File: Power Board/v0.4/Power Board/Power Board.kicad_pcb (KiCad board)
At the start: 4 copper layers, 70 x 80 mm, 84 parts, among them J1 Battery In, J2 JST B2PS-VH, J3 JST B2PS-VH, J4 JST B2PS-VH, J5 JST B2PS-VH, J6 JST B2PS-VH, J7 JST B2PS-VH, J9 Raspberry Pi, Q1 SI5504BDC, SW1 SW_Push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

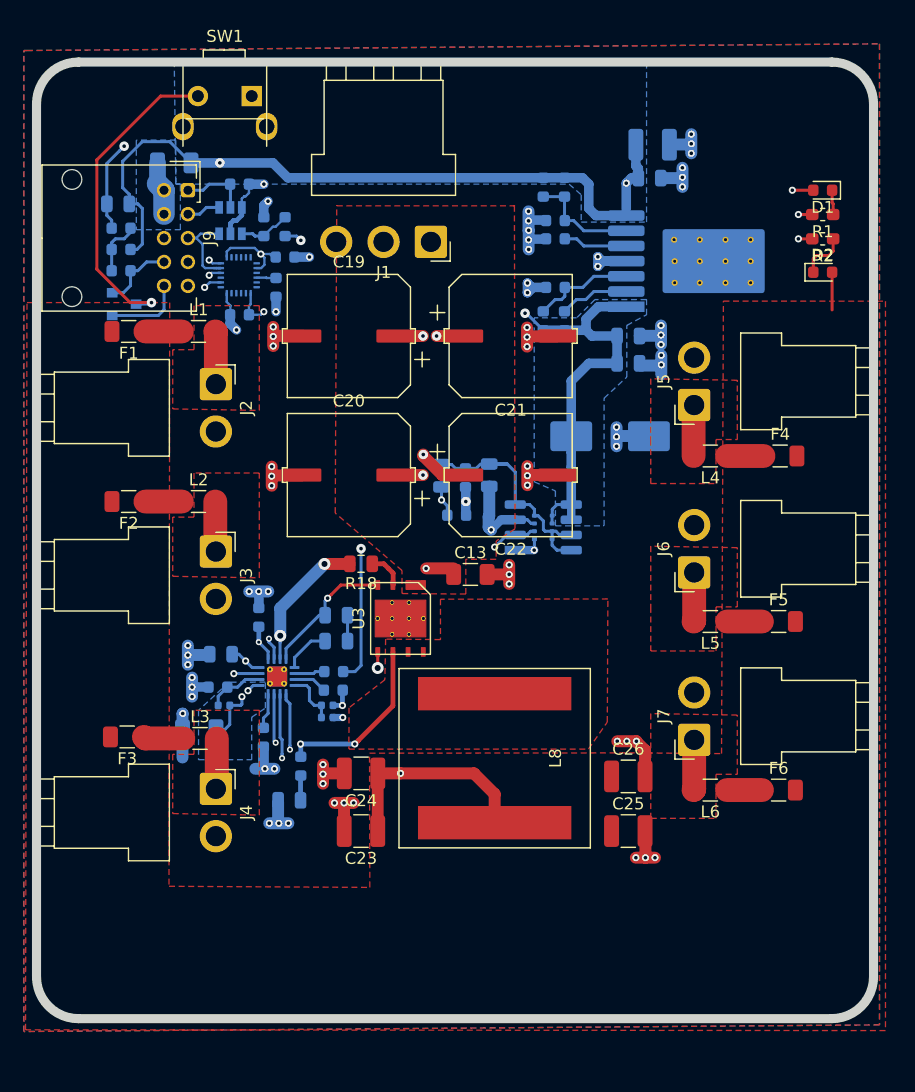
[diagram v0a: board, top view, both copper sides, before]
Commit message: Better ground flow through Q1 Need to add more copper for panel connector between fuse and ferrite
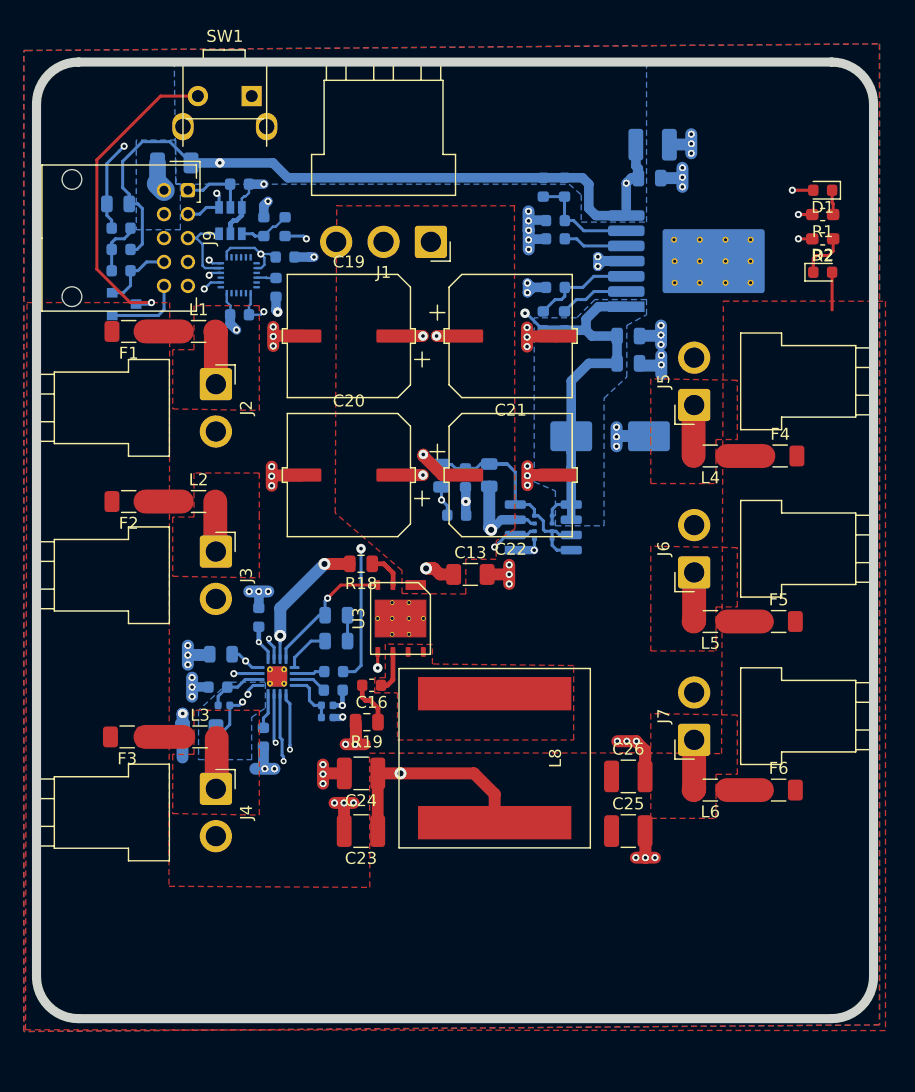
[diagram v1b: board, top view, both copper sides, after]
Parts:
- C16, R19: moved to F.Cu
- moved R19 9.20 mm to (104.6, 90.2)
- moved C16 8.99 mm to (105.0, 87.1), turned to 180 degrees
- moved L3 0.13 mm to (90.7, 91.4)
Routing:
- net SDA: track 78.1 -> 89.3 mm, vias 2 -> 3
- net /Panel Power/Switch_Node: track 14.7 -> 3.52 mm, vias 2 -> 0
- net Net-(C16-Pad2): track 2.60 -> 3.85 mm
- net /Panel_Power: track 43.3 -> 42.4 mm
- net /Battery_Power: track 45.9 -> 46.7 mm
- net Net-(C1-Pad1): track 21.5 -> 22.2 mm
- net GND: track 108.8 -> 109.4 mm, vias 76 -> 75

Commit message: Changed connections to panel connectors. Did some of the TLC work on the pours. Still need to fix DRC, mostly for U2 clearance issues that aren't really a DRC
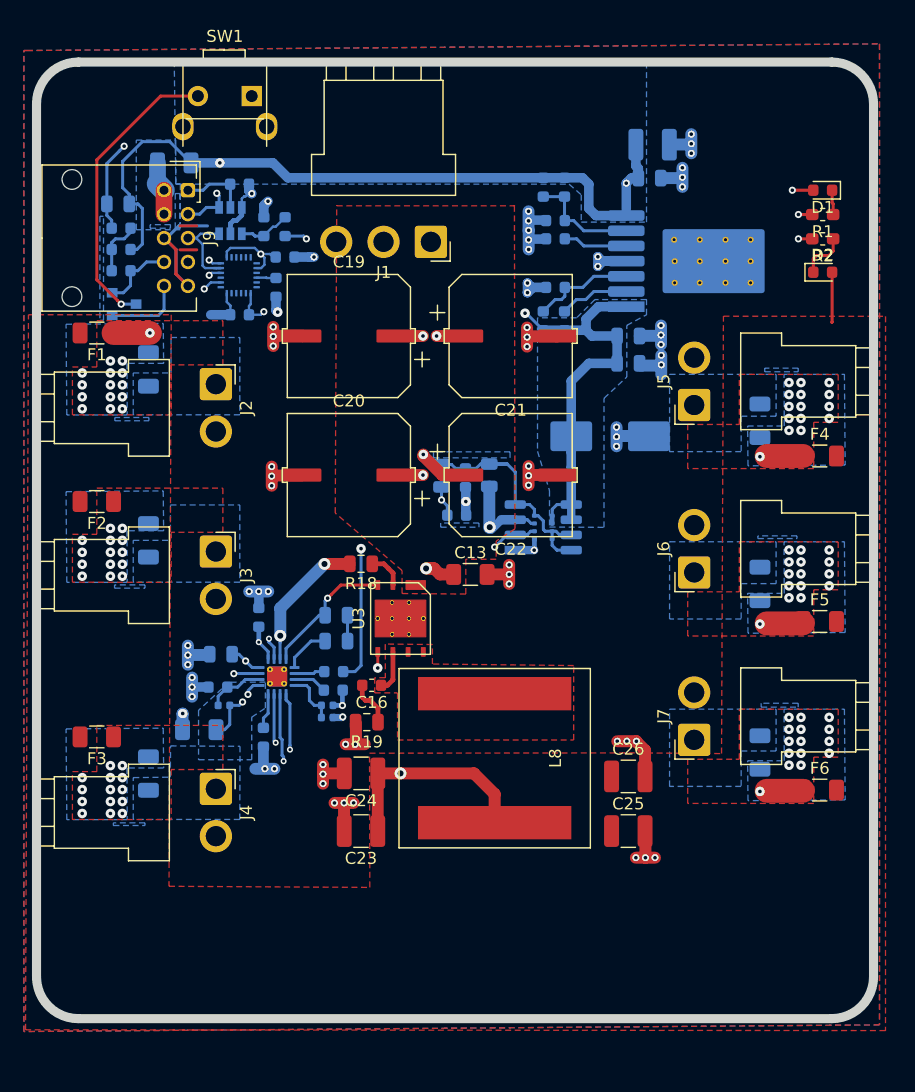
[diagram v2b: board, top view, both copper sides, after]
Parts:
- L1, L2, L3, L4, L5, L6: moved to B.Cu
- moved L2 5.30 mm to (86.4, 75.0), turned to 270 degrees
- moved L3 5.29 mm to (86.4, 94.5), turned to 270 degrees
- moved L1 5.26 mm to (86.4, 60.7), turned to 270 degrees
- moved L5 5.21 mm to (137.5, 78.6), turned to 90 degrees
- moved L6 5.21 mm to (137.5, 92.7), turned to 90 degrees
- moved L4 5.09 mm to (137.5, 65.0), turned to 90 degrees
- moved F5 3.44 mm to (142.5, 81.8)
- moved F6 3.44 mm to (142.5, 95.9)
- moved F4 3.31 mm to (142.5, 67.9)
- moved F1 2.67 mm to (82.0, 57.7)
- moved F2 2.67 mm to (82.0, 71.8)
- moved F3 2.54 mm to (82.0, 91.4)
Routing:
- net GND: track 109.4 -> 123.6 mm, vias 75 -> 74
- net Net-(J2-Pad1): track 4.43 -> 0.00 mm
- net Net-(J7-Pad1): track 4.22 -> 0.00 mm
- net Net-(J5-Pad1): track 4.28 -> 0.07 mm
- net Net-(J4-Pad1): track 4.24 -> 0.11 mm
- net Net-(J3-Pad1): track 4.20 -> 0.07 mm
- net Net-(J6-Pad1): track 4.12 -> 0.00 mm
- net Net-(F3-Pad1): track 3.17 -> 0.00 mm, vias 0 -> 14
- net Net-(F2-Pad1): track 3.04 -> 0.00 mm, vias 0 -> 14
- net /Pi Power/Power_Button: track 73.0 -> 70.9 mm
- net SCL: track 70.7 -> 68.9 mm
- net /Panel_Alert: track 57.6 -> 56.2 mm
- net /Panel_Power: track 42.4 -> 43.5 mm
- net SDA: track 89.3 -> 89.9 mm
- net Net-(F6-Pad1): track 2.91 -> 3.04 mm, vias 0 -> 15
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- added copper zone on B.Cu, net Net-(F1-Pad1)
- added copper zone on F.Cu, net Net-(F1-Pad1)
- added copper zone on B.Cu, net Net-(F2-Pad1)
- added copper zone on F.Cu, net Net-(F2-Pad1)
- added copper zone on B.Cu, net Net-(F3-Pad1)
- added copper zone on F.Cu, net Net-(F3-Pad1)
- added copper zone on B.Cu, net Net-(F4-Pad1)
- added copper zone on F.Cu, net Net-(F4-Pad1)
- added copper zone on B.Cu, net Net-(F5-Pad1)
- added copper zone on F.Cu, net Net-(F5-Pad1)
- added copper zone on B.Cu, net Net-(F6-Pad1)
- added copper zone on F.Cu, net Net-(F6-Pad1)
- added copper zone on B.Cu, net Net-(J2-Pad1)
- added copper zone on B.Cu, net Net-(J3-Pad1)
- added copper zone on B.Cu, net Net-(J4-Pad1)
- added copper zone on B.Cu, net Net-(J5-Pad1)
- added copper zone on B.Cu, net Net-(J6-Pad1)
- added copper zone on B.Cu, net Net-(J7-Pad1)
- removed copper zone on F.Cu, net Net-(J2-Pad1)
- removed copper zone on F.Cu, net Net-(J3-Pad1)
- removed copper zone on F.Cu, net Net-(J4-Pad1)
- removed copper zone on F.Cu, net Net-(J5-Pad1)
- removed copper zone on F.Cu, net Net-(J6-Pad1)
- removed copper zone on F.Cu, net Net-(J7-Pad1)
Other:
- net class U2 removed

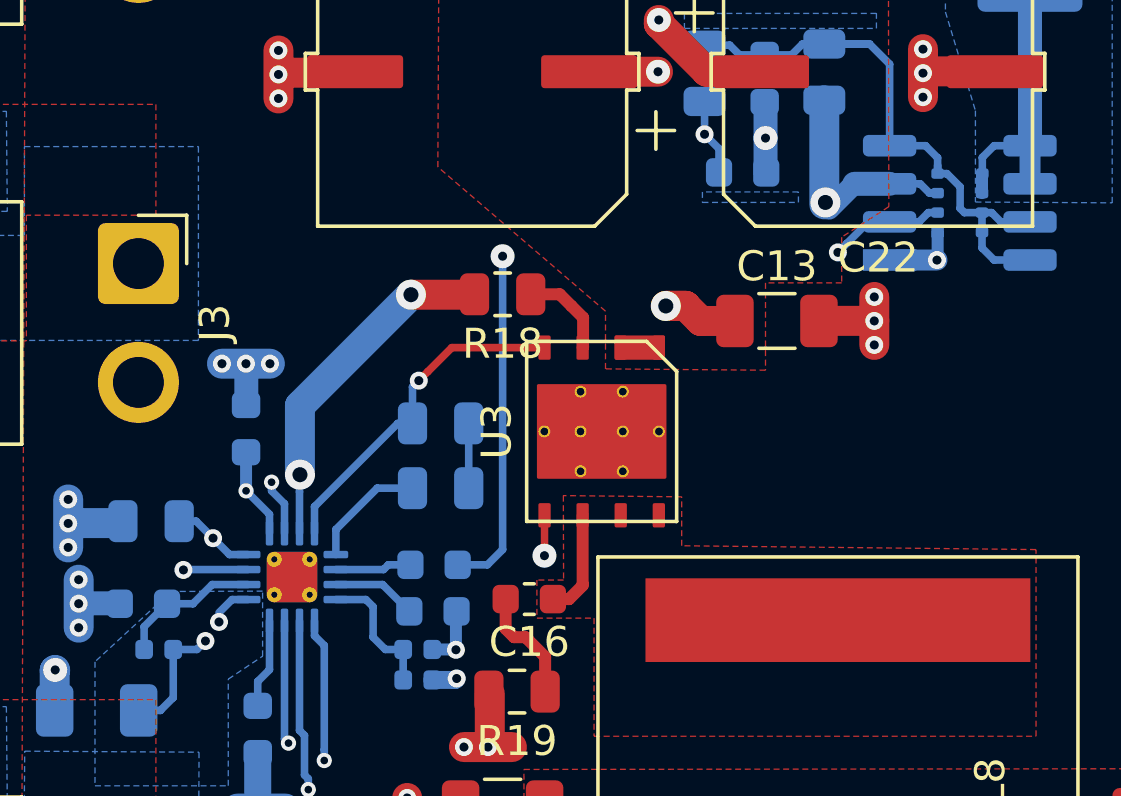
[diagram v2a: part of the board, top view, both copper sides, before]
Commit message: Tracks and rules tweaked to eliminate most DRC 2 DRC errors remain which don't seem valid
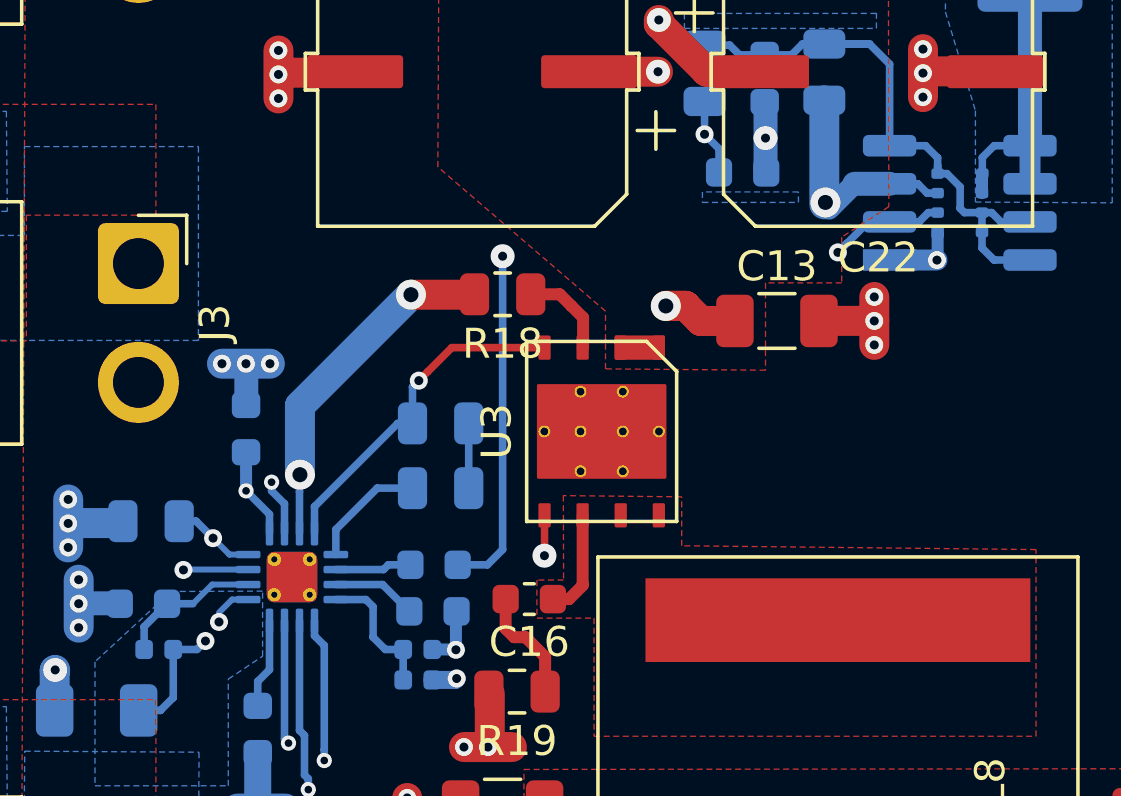
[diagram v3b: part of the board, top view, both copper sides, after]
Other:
- net class Pi_Battery: clearance 0.3 -> 0.25
- net class Pi_Power: clearance 0.3 -> 0.25
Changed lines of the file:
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@@
     (mod_text_size 1 1)
     (mod_text_width 0.15)
-    (pad_size 0.25 0.825)
-    (pad_drill 0)
+    (pad_size 0.45 0.45)
+    (pad_drill 0.2)
     (pad_to_mask_clearance 0.0508)
     (solder_mask_min_width 0.25)
@@
   )
   (net_class Pi_Battery ""
-    (clearance 0.3)
+    (clearance 0.25)
     (trace_width 0.3)
     (via_dia 1)
@@
   )
   (net_class Pi_Power ""
-    (clearance 0.3)
+    (clearance 0.25)
     (trace_width 1.4)
     (via_dia 1)
@@
     (pad 17 smd roundrect (at 0 0 90) (size 1.68 1.68) (layers F.Cu) (roundrect_rratio 0.14881)
       (net 4 GND) (zone_connect 2))
-    (pad 17 thru_hole circle (at 0.59 -0.59 90) (size 0.5 0.5) (drill 0.2) (layers *.Cu)
+    (pad 17 thru_hole circle (at 0.59 -0.59 90) (size 0.45 0.45) (drill 0.2) (layers *.Cu)
       (net 4 GND) (zone_connect 2))
-    (pad 17 thru_hole circle (at -0.59 -0.59 90) (size 0.5 0.5) (drill 0.2) (layers *.Cu)
+    (pad 17 thru_hole circle (at -0.59 -0.59 90) (size 0.45 0.45) (drill 0.2) (layers *.Cu)
       (net 4 GND) (zone_connect 2))
-    (pad 17 thru_hole circle (at 0.59 0.59 90) (size 0.5 0.5) (drill 0.2) (layers *.Cu)
+    (pad 17 thru_hole circle (at 0.59 0.59 90) (size 0.45 0.45) (drill 0.2) (layers *.Cu)
       (net 4 GND) (zone_connect 2))
-    (pad 17 thru_hole circle (at -0.59 0.59 90) (size 0.5 0.5) (drill 0.2) (layers *.Cu)
+    (pad 17 thru_hole circle (at -0.59 0.59 90) (size 0.45 0.45) (drill 0.2) (layers *.Cu)
       (net 4 GND) (zone_connect 2))
     (pad 17 smd roundrect (at 0 0 90) (size 1.68 1.68) (layers B.Cu B.Mask) (roundrect_rratio 0.14881)
@@
   (segment (start 107.024 57.912) (end 109.32 57.912) (width 1) (layer F.Cu) (net 3))
   (segment (start 107.024 69.542) (end 109.32 69.542) (width 1) (layer F.Cu) (net 3))
-  (segment (start 118.0592 73.279) (end 117.04 73.279) (width 0.254) (layer B.Cu) (net 3))
-  (segment (start 118.3692 73.589) (end 118.0592 73.279) (width 0.254) (layer B.Cu) (net 3))
-  (segment (start 118.64 73.589) (end 118.3692 73.589) (width 0.254) (layer B.Cu) (net 3))
   (via (at 114.9 73.9) (size 1) (drill 0.5) (layers F.Cu B.Cu) (net 3))
   (segment (start 114.8005 70.556) (end 114.863 70.4935) (width 0.8) (layer B.Cu) (net 3))
   (segment (start 115.865 73.279) (end 115.022 74.122) (width 0.7) (layer B.Cu) (net 3))
   (segment (start 93.923 84.525) (end 93.3585 84.525) (width 0.254) (layer B.Cu) (net 3))
-  (segment (start 95.035 85.637) (end 94.488 85.09) (width 0.254) (layer B.Cu) (net 3))
-  (segment (start 95.6565 85.637) (end 95.035 85.637) (width 0.254) (layer B.Cu) (net 3))
+  (segment (start 95.035 85.637) (end 94.488 85.09) (width 0.2) (layer B.Cu) (net 3))
+  (segment (start 95.6565 85.637) (end 95.035 85.637) (width 0.2) (layer B.Cu) (net 3))
   (segment (start 94.488 85.09) (end 93.923 84.525) (width 0.254) (layer B.Cu) (net 3))
   (via (at 94.488 85.09) (size 0.6) (drill 0.3) (layers F.Cu B.Cu) (net 3))
@@
   (segment (start 110.744 77.851) (end 111.884 77.851) (width 1) (layer F.Cu) (net 3))
   (segment (start 110.244 77.351) (end 110.744 77.851) (width 1) (layer F.Cu) (net 3))
+  (segment (start 117.979 73.279) (end 117.04 73.279) (width 0.254) (layer B.Cu) (net 3))
+  (segment (start 118.289 73.589) (end 117.979 73.279) (width 0.254) (layer B.Cu) (net 3))
+  (segment (start 118.64 73.589) (end 118.289 73.589) (width 0.254) (layer B.Cu) (net 3))
   (via (at 118.618 75.822) (size 0.6) (drill 0.3) (layers F.Cu B.Cu) (net 4))
   (segment (start 118.618 75.819) (end 117.268 75.819) (width 0.7) (layer B.Cu) (net 4))
@@
   (segment (start 95.977 92.384487) (end 95.977 93.982513) (width 0.9) (layer B.Cu) (net 4))
   (segment (start 93.513 86.137) (end 93.5 86.15) (width 0.254) (layer B.Cu) (net 4))
-  (segment (start 95.6565 86.137) (end 93.513 86.137) (width 0.254) (layer B.Cu) (net 4))
+  (segment (start 95.6565 86.137) (end 93.513 86.137) (width 0.2) (layer B.Cu) (net 4))
   (segment (start 96.012 47.9805) (end 96.012 46.99) (width 0.8) (layer B.Cu) (net 4))
   (segment (start 96.012 46.99) (end 96.358205 46.643795) (width 0.8) (layer B.Cu) (net 4))
@@
   (segment (start 92.734 90.833) (end 93.16 90.407) (width 0.254) (layer B.Cu) (net 13))
   (segment (start 92.009 90.833) (end 92.734 90.833) (width 0.254) (layer B.Cu) (net 13))
-  (segment (start 95.122 87.137) (end 95.6565 87.137) (width 0.254) (layer B.Cu) (net 13))
+  (segment (start 95.122 87.137) (end 95.6565 87.137) (width 0.2) (layer B.Cu) (net 13))
   (segment (start 115.316 98.613) (end 115.316 96.218) (width 1) (layer F.Cu) (net 13))
   (segment (start 115.316 96.218) (end 113.586 94.488) (width 1) (layer F.Cu) (net 13))
@@
   (segment (start 105.534 94.494) (end 105.54 94.488) (width 1) (layer F.Cu) (net 13))
   (segment (start 105.534 99.314) (end 105.534 94.494) (width 1) (layer F.Cu) (net 13))
-  (segment (start 94.6855 87.5735) (end 95.122 87.137) (width 0.254) (layer B.Cu) (net 13))
+  (segment (start 94.6855 87.5735) (end 95.122 87.137) (width 0.2) (layer B.Cu) (net 13))
   (via (at 94.6855 87.884) (size 0.6) (drill 0.3) (layers F.Cu B.Cu) (net 13))
   (segment (start 107.442 94.488) (end 105.54 94.488) (width 1) (layer F.Cu) (net 13))
@@
   (segment (start 99.96 83.424) (end 98.5815 84.8025) (width 0.254) (layer B.Cu) (net 38))
   (segment (start 101.1355 83.424) (end 99.96 83.424) (width 0.254) (layer B.Cu) (net 38))
-  (segment (start 95.6565 86.637) (end 94.458 86.637) (width 0.254) (layer B.Cu) (net 39))
-  (segment (start 94.458 86.637) (end 93.818 87.277) (width 0.254) (layer B.Cu) (net 39))
+  (segment (start 95.6565 86.637) (end 94.458 86.637) (width 0.2) (layer B.Cu) (net 39))
+  (segment (start 94.458 86.637) (end 93.818 87.277) (width 0.2) (layer B.Cu) (net 39))
   (segment (start 93.818 87.277) (end 92.9545 87.277) (width 0.254) (layer B.Cu) (net 39))
   (segment (start 92.19 88.0415) (end 92.9545 87.277) (width 0.254) (layer B.Cu) (net 39))
